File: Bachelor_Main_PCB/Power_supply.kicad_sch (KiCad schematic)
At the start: 53 parts, among them IC1 LD3985M18R, J22 691137710002, J23 691137710002, J24 Conn_01x03_Pin, Q4 BC817-40Q-13-F, U10 LMR51450FNDRRR, U11 LMR51450FNDRRR, U9 LM73100RPWR

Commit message: Standardized on "." for decimal spaces
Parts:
- L2: value 4,7uH -> 4.7uH
- L3: value 3,3uH -> 3.3uH
- R12: value 86k6 -> 86.6k
- R14: value 2k26 -> 2.26k
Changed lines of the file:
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@@
 			)
 		)
-		(property "Value" "4,7uH"
+		(property "Value" "4.7uH"
 			(at 214.122 26.416 0)
 			(effects
@@
 			)
 		)
-		(property "Value" "86k6"
+		(property "Value" "86.6k"
 			(at 48.26 38.0999 0)
 			(effects
@@
 			)
 		)
-		(property "Value" "3,3uH"
+		(property "Value" "3.3uH"
 			(at 213.36 81.026 0)
 			(effects
@@
 			)
 		)
-		(property "Value" "2k26"
+		(property "Value" "2.26k"
 			(at 101.6 39.37 0)
 			(effects

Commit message: Fixed DRC, footprints and power flags and no-connect flags
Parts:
- IC1: footprint SOT95P280X145-5N -> KiCad5:SOT95P280X145-5N
- Q4: footprint SOT96P240X110-3N -> KiCad7:SOT96P240X110-3N
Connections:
- no-connect marks 3 -> 5

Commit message: Fix all DRC errors and warnings
except not connected pins still unrouted to MCU
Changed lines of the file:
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@@
 	)
 	(junction
+		(at 22.86 38.1)
+		(diameter 0)
+		(color 0 0 0 0)
+	)
+	(junction
 		(at 45.72 40.64)
 		(diameter 0)
@@
 	(wire
 		(pts
-			(xy 22.86 29.21) (xy 22.86 27.94)
+			(xy 22.86 39.37) (xy 22.86 38.1)
 		)
 		(stroke
@@
 	(wire
 		(pts
+			(xy 22.86 38.1) (xy 22.86 27.94)
+		)
+		(stroke
+			(width 0)
+			(type default)
+		)
+	)
+	(wire
+		(pts
 			(xy 99.06 139.7) (xy 99.06 144.78)
 		)
@@
 	)
 	(symbol
+		(lib_id "power:PWR_FLAG")
+		(at 22.86 38.1 90)
+		(unit 1)
+		(exclude_from_sim no)
+		(in_bom yes)
+		(on_board yes)
+		(dnp no)
+		(property "Reference" "#FLG016"
+			(at 20.955 38.1 0)
+			(effects
+				(font
+					(size 1.27 1.27)
+				)
+				(hide yes)
+			)
+		)
+		(property "Value" "PWR_FLAG"
+			(at 15.24 38.354 90)
+			(effects
+				(font
+					(size 1.27 1.27)
+				)
+			)
+		)
+		(property "Footprint" ""
+			(at 22.86 38.1 0)
+			(effects
+				(font
+					(size 1.27 1.27)
+				)
+				(hide yes)
+			)
+		)
+		(property "Datasheet" "~"
+			(at 22.86 38.1 0)
+			(effects
+				(font
+					(size 1.27 1.27)
+				)
+				(hide yes)
+			)
+		)
+		(property "Description" "Special symbol for telling ERC where power comes from"
+			(at 22.86 38.1 0)
+			(effects
+				(font
+					(size 1.27 1.27)
+				)
+				(hide yes)
+			)
+		)
+		(pin "1"
+		)
+		(instances
+			(project ""
+				(path "/3544d663-329e-4884-b753-28436ca187e8/4408de3e-a395-4433-a2e1-ccefac59f96e"
+					(reference "#FLG016")
+					(unit 1)
+				)
+			)
+		)
+	)
+	(symbol
 		(lib_id "Device:R_Small")
 		(at 158.75 40.64 0)
@@
 	(symbol
 		(lib_id "power:GND")
-		(at 22.86 29.21 0)
+		(at 22.86 39.37 0)
 		(unit 1)
 		(exclude_from_sim no)
@@
 		(fields_autoplaced yes)
 		(property "Reference" "#PWR076"
-			(at 22.86 35.56 0)
+			(at 22.86 45.72 0)
 			(effects
 				(font
@@
 		)
 		(property "Value" "GND"
-			(at 22.86 34.29 0)
+			(at 22.86 44.45 0)
 			(effects
 				(font
@@
 		)
 		(property "Footprint" ""
-			(at 22.86 29.21 0)
+			(at 22.86 39.37 0)
 			(effects
 				(font
@@
 		)
 		(property "Datasheet" ""
-			(at 22.86 29.21 0)
+			(at 22.86 39.37 0)
 			(effects
 				(font
@@
 		)
 		(property "Description" "Power symbol creates a global label with name \"GND\" , ground"
-			(at 22.86 29.21 0)
+			(at 22.86 39.37 0)
 			(effects
 				(font

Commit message: Imported components from schematic to PCB and Reanotat all designators
THis means every designator is now different and the references made prior no longer applies
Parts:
- renumbered C49 to C38, C62 to C39, C59 to C40, C45 to C41, C44 to C42, C53 to C43, C51 to C44, C52 to C45, C50 to C46, C48 to C47, C54 to C48, C60 to C49, C61 to C50, C56 to C51, C57 to C52, C58 to C53, C55 to C54, C64 to C55, C65 to C56, C63 to C57, C47 to C58, C46 to C59, D5 to D11, D9 to D12, J23 to J26, J24 to J27, J22 to J28, L5 to L2, L2 to L3, L3 to L5, Q4 to Q13, R11 to R40, R22 to R41, R23 to R42, R12 to R43, R14 to R44, R18 to R45, R13 to R46, R20 to R47, R15 to R48, R17 to R49, R16 to R50, R26 to R51, R25 to R52, R24 to R53, R27 to R54, R19 to R55, R30 to R56, U11 to U10, U9 to U8, U10 to U9

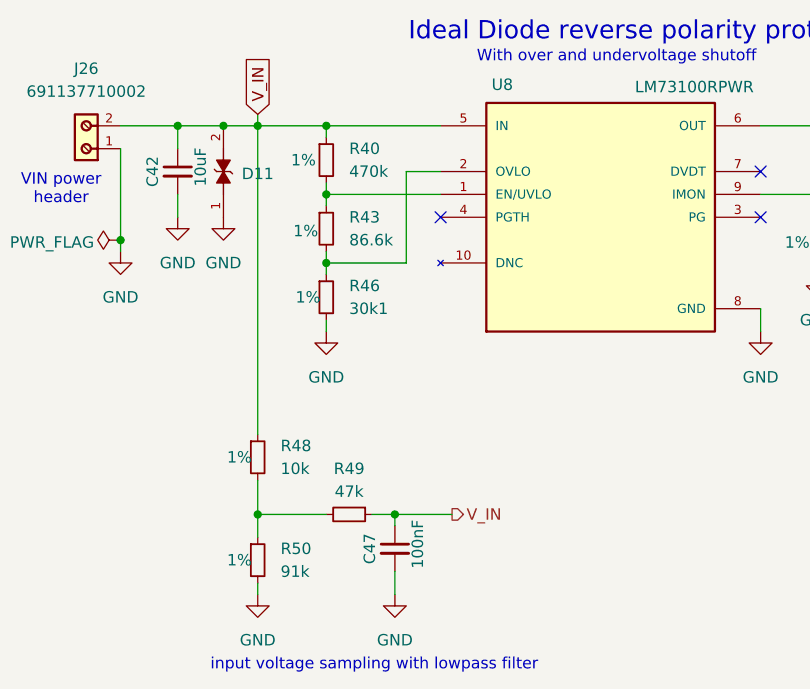
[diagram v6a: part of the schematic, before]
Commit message: Changed V_IN on adc mcu sense pin to V_VIN_MEAS
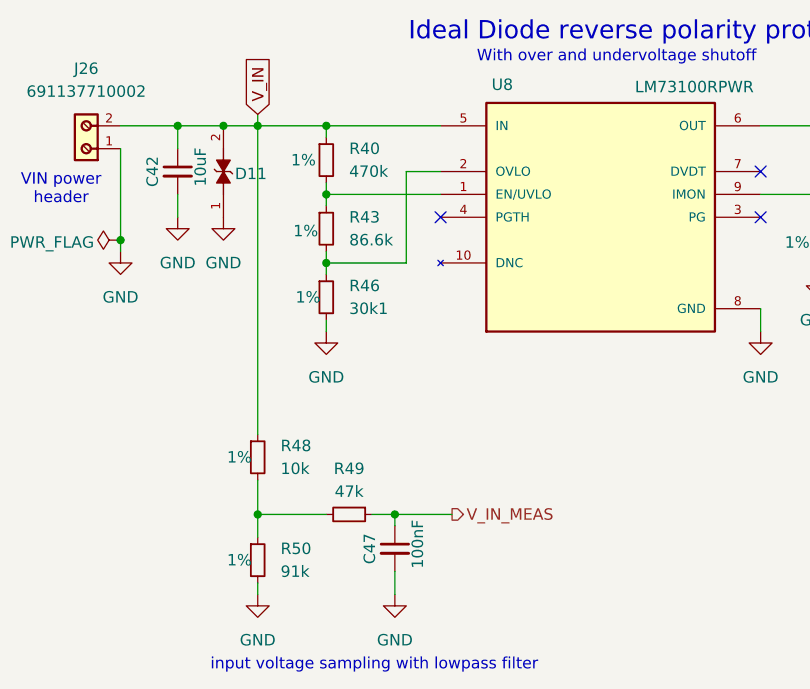
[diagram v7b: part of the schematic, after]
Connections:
- net V_IN: no longer C47.1, R49.1
- new net V_IN_MEAS: C47.1, R49.1
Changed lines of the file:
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@@
 		)
 	)
-	(hierarchical_label "V_IN"
+	(hierarchical_label "V_IN_MEAS"
 		(shape output)
 		(at 59.69 68.58 0)
@@
 		(dnp no)
 		(property "Reference" "D11"
-			(at 36.322 30.734 90)
+			(at 35.56 30.734 90)
 			(effects
 				(font

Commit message: Text from meeting with julia
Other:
- note added: "FIX THIS!!!!!"
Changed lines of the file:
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@@
+		)
+	)
+	(text "FIX THIS!!!!!"
+		(exclude_from_sim no)
+		(at 37.084 66.802 0)
+		(effects
+			(font
+				(size 1.27 1.27)
+			)
 		)
 	)
